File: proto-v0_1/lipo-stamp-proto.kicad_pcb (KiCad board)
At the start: 4 copper layers, 45.7 x 45.7 mm, 110 parts, among them Q1 Q_PMOS_GSD, U3 MCP73832-2-OT, U4 AP2112K-3.3, U5 AP9101CK6, U6 FS8205

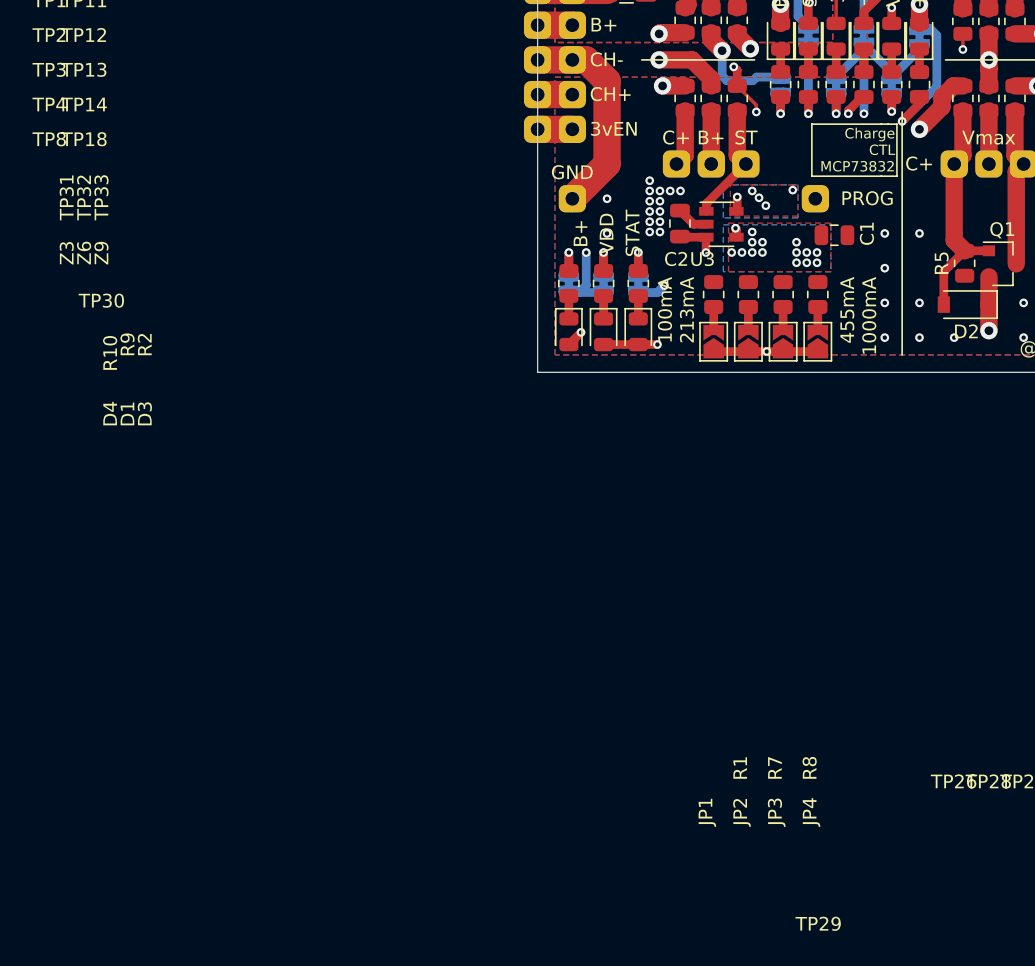
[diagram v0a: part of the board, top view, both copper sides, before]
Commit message: Rerouted TP4056, considering redoing
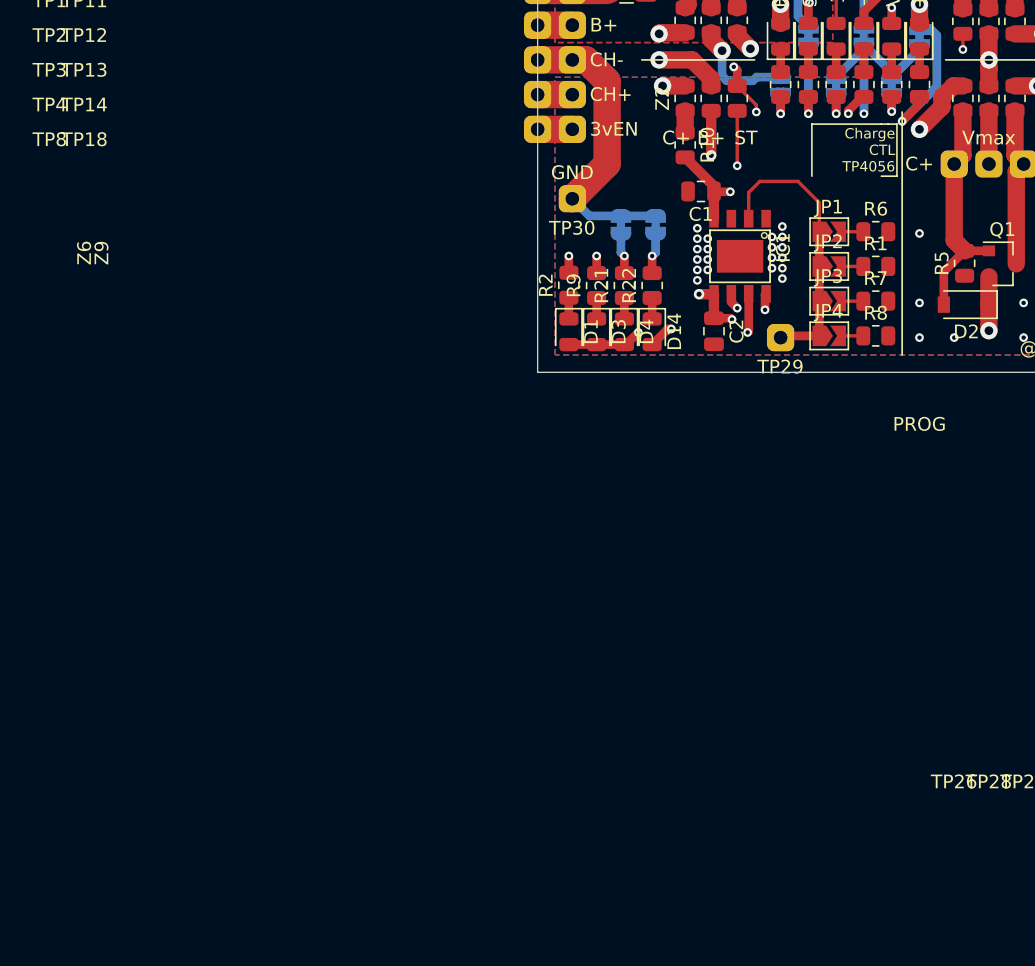
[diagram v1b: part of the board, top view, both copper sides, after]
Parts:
- removed JP7: Jumper_NC_Small, Jumper:SolderJumper-2_P1.3mm_Bridged_RoundedPad1.0x1.5mm
- removed TP31, TP32, TP33: TestPoint, Everything:castellated-2-pin
- removed U3: MCP73832-2-OT, Package_TO_SOT_SMD:SOT-23-5
- removed Z3: 0, Resistor_SMD:R_0805_2012Metric
- added D14: LED, LED_SMD:LED_0805_2012Metric, F.Cu at (186.2, 93.6)
- added IC1: TP4056, Everything:SOP-8, F.Cu at (192.6, 88.0)
- added R21: R, Resistor_SMD:R_0805_2012Metric, F.Cu at (184.2, 90.2)
- added R22: R, Resistor_SMD:R_0805_2012Metric, F.Cu at (186.2, 90.2)
- added Z2: 0, Resistor_SMD:R_0805_2012Metric, F.Cu at (188.6, 76.5)
- C1, C2: value 4.7uF -> 10uF
- R10: value R -> 0.4
- R8: value 1K -> 1K2
- moved R10 13.2 mm to (188.6, 79.9), turned to 270 degrees
- moved R6 12.7 mm to (202.5, 86.2), turned to 0 degrees
- moved JP1 11.7 mm to (199.1, 86.2), turned to 0 degrees
- moved TP29 10.5 mm to (195.6, 94.0)
- moved C1 10.3 mm to (189.8, 83.3), turned to 180 degrees
- moved R1 9.55 mm to (202.5, 88.8), turned to 0 degrees
- moved C2 8.26 mm to (190.7, 93.5), turned to 270 degrees
- moved JP2 8.08 mm to (199.1, 88.8), turned to 0 degrees
- moved R7 6.80 mm to (202.5, 91.3), turned to 0 degrees
- moved R8 5.21 mm to (202.5, 93.9), turned to 0 degrees
- moved R2 5.08 mm to (180.1, 90.1)
- moved JP6 4.50 mm to (186.4, 85.7), turned to 270 degrees
- moved JP3 4.49 mm to (199.1, 91.3), turned to 0 degrees
- moved JP5 4.49 mm to (183.9, 85.7), turned to 270 degrees
- moved D4 4.06 mm to (184.2, 93.6)
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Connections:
- D4 pad 2: Net-(C2-Pad1) -> Net-(C1-Pad1)
- JP6 pad 1: Net-(JP6-Pad1) -> GND
- R10 pad 1: Net-(D4-Pad1) -> Net-(R10-Pad1)
- R10 pad 2: Net-(JP7-Pad2) -> Net-(C1-Pad1)
- R2 pad 1: Net-(D3-Pad1) -> Net-(D1-Pad1)
- R2 pad 2: Net-(JP6-Pad2) -> Net-(IC1-Pad6)
- R9 pad 1: Net-(D1-Pad1) -> Net-(D3-Pad1)
- R9 pad 2: Net-(JP5-Pad2) -> Net-(IC1-Pad7)
- Z6 pad 1: Net-(JP6-Pad1) -> Net-(IC1-Pad7)
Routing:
- net Net-(IC1-Pad7): track 0.00 -> 39.5 mm, vias 0 -> 3
- net Net-(JP6-Pad1): track 28.2 -> 0.00 mm, vias 1 -> 0
- net Net-(IC1-Pad6): track 0.00 -> 16.3 mm, vias 0 -> 2
- net Net-(C1-Pad1): track 26.4 -> 34.7 mm, vias 16 -> 3
- net Net-(IC1-Pad2): track 26.8 -> 20.7 mm, vias 6 -> 0
- net Net-(JP7-Pad2): track 2.97 -> 0.00 mm, vias 1 -> 0
- net GND: track 69.1 -> 66.9 mm
- net Net-(R10-Pad1): track 0.00 -> 1.58 mm
- net Net-(D14-Pad1): track 0.00 -> 1.53 mm
- net Net-(C2-Pad1): track 26.4 -> 25.4 mm, vias 2 -> 4
- removed copper zone on B.Cu, net Net-(C1-Pad1)
- removed copper zone on F.Cu, net Net-(C1-Pad1)
- removed copper zone on B.Cu, net Net-(IC1-Pad2)
- removed copper zone on F.Cu, net Net-(IC1-Pad2)
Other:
- board text added: "Charge CTL TP4056"
- board text removed: "100mA 213mA"
- board text removed: "455mA 1000mA"
- board text removed: "Charge CTL MCP73832"
